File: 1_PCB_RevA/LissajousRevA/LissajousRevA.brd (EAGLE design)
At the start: 100 x 80 mm, 77 parts, among them U101 LM348D, U201 LM348D, U401 LM348D

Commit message: quick route
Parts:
- moved C505 6.35 mm to (17.8, 16.5)
- moved C504 5.39 mm to (12.7, 16.5)
- moved Q503 4.58 mm to (22.9, 16.5)
- moved R508 2.54 mm to (12.7, 22.9)
- moved R509 2.54 mm to (7.62, 22.9), turned to 270 degrees
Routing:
- net N$39: track 28.0 -> 6.56 mm, vias 2 -> 0
- net N$46: track 30.3 -> 17.8 mm
- net N$45: track 23.9 -> 14.6 mm
- net N$40: track 11.1 -> 7.90 mm
- net N$38: track 158.6 -> 156.3 mm
- net N$42: track 43.5 -> 42.0 mm
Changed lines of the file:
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@@
 <element name="R506" library="passives" package="0603-RES" value="33K" x="53.34" y="29.21" rot="R90"/>
 <element name="Q502" library="adafruit" package="SOT23" value="" x="53.34" y="48.26" rot="R90"/>
-<element name="C504" library="passives" package="0603-CAP" value="10nF" x="8.89" y="20.32" rot="R270"/>
+<element name="C504" library="passives" package="0603-CAP" value="10nF" x="12.7" y="16.51" rot="R270"/>
 <element name="R507" library="passives" package="0603-RES" value="33K" x="38.1" y="16.51" rot="R90"/>
-<element name="C505" library="passives" package="0603-CAP" value="10nF" x="12.7" y="20.32" rot="R90"/>
-<element name="Q503" library="adafruit" package="SOT23" value="" x="19.05" y="13.97" rot="R90"/>
-<element name="R508" library="passives" package="0603-RES" value="33K" x="12.7" y="25.4" rot="R90"/>
-<element name="R509" library="passives" package="0603-RES" value="33K" x="7.62" y="25.4" rot="R90"/>
+<element name="C505" library="passives" package="0603-CAP" value="10nF" x="17.78" y="16.51" rot="R90"/>
+<element name="Q503" library="adafruit" package="SOT23" value="" x="22.86" y="16.51" rot="R90"/>
+<element name="R508" library="passives" package="0603-RES" value="33K" x="12.7" y="22.86" rot="R90"/>
+<element name="R509" library="passives" package="0603-RES" value="33K" x="7.62" y="22.86" rot="R270"/>
 <element name="R510" library="passives" package="0603-RES" value="33K" x="7.62" y="50.8" rot="R270"/>
 <element name="TP305" library="passives" package="TP_15TH" value="TEST-POINTTP_15TH_THRU" x="2.54" y="41.91"/>
@@
 <wire x1="88.9" y1="31.75" x2="88.9" y2="44.45" width="0.4064" layer="16"/>
 <wire x1="88.9" y1="44.45" x2="86.36" y2="46.99" width="0.4064" layer="16"/>
-<wire x1="33.02" y1="26.67" x2="33.02" y2="26.67" width="0" layer="19" extent="1-16"/>
-<wire x1="33.02" y1="26.67" x2="33.02" y2="29.21" width="0" layer="19" extent="1-16"/>
-<wire x1="33.02" y1="29.21" x2="36.83" y2="33.02" width="0" layer="19" extent="1-16"/>
 <via x="36.83" y="33.02" extent="1-16" drill="0.6"/>
 <wire x1="17.78" y1="35.4838" x2="17.78" y2="39.79" width="0.4064" layer="1"/>
 <wire x1="17.78" y1="39.79" x2="16.09" y2="39.79" width="0.4064" layer="1"/>
 <wire x1="16.09" y1="39.79" x2="15.24" y2="40.64" width="0.4064" layer="1"/>
-<wire x1="33.02" y1="29.21" x2="33.02" y2="31.75" width="0" layer="19" extent="1-16"/>
 <wire x1="33.02" y1="31.75" x2="31.75" y2="33.02" width="0.4064" layer="16"/>
 <wire x1="31.75" y1="33.02" x2="6.35" y2="33.02" width="0.4064" layer="16"/>
@@
 <wire x1="33.02" y1="3.81" x2="35.56" y2="1.27" width="0.4064" layer="1"/>
 <wire x1="35.56" y1="1.27" x2="55.88" y2="1.27" width="0.4064" layer="1"/>
-<wire x1="33.02" y1="3.81" x2="33.02" y2="26.67" width="0" layer="19" extent="1-1"/>
+<wire x1="33.02" y1="31.75" x2="36.83" y2="33.02" width="0" layer="19" extent="16-16"/>
+<wire x1="68.58" y1="41.06" x2="43.18" y2="38.1" width="0" layer="19" extent="1-1"/>
 </signal>
 <signal name="0V">
@@
 <wire x1="34.29" y1="42.76" x2="34.29" y2="43.18" width="0" layer="19" extent="1-1"/>
 <wire x1="38.1" y1="15.66" x2="34.29" y2="20.32" width="0" layer="19" extent="1-1"/>
-<wire x1="20.15" y1="14.92" x2="34.29" y2="20.32" width="0" layer="19" extent="1-1"/>
-<wire x1="17.78" y1="21.59" x2="20.15" y2="14.92" width="0" layer="19" extent="1-1"/>
+<wire x1="23.96" y1="17.46" x2="34.29" y2="20.32" width="0" layer="19" extent="1-1"/>
+<wire x1="17.78" y1="21.59" x2="23.96" y2="17.46" width="0" layer="19" extent="1-1"/>
 </signal>
 <signal name="N$8">
@@
 <wire x1="17.78" y1="26.25" x2="20.32" y2="28.79" width="0.4064" layer="1"/>
 <wire x1="20.32" y1="28.79" x2="20.32" y2="30.5562" width="0.4064" layer="1"/>
-<wire x1="24.13" y1="26.25" x2="17.78" y2="26.25" width="0" layer="19" extent="1-16"/>
-<wire x1="19.05" y1="24.98" x2="24.55" y2="26.25" width="0" layer="19" extent="1-16"/>
-<wire x1="24.55" y1="26.25" x2="24.13" y2="26.25" width="0" layer="19" extent="1-1"/>
+<wire x1="19.05" y1="24.98" x2="17.78" y2="26.25" width="0" layer="19" extent="1-1"/>
 </signal>
 <signal name="N$15">
@@
 <contactref element="U401" pad="14"/>
 <contactref element="C504" pad="2"/>
-<wire x1="8.89" y1="19.47" x2="8.89" y2="17.78" width="0.4064" layer="1"/>
-<wire x1="8.89" y1="17.78" x2="10.16" y2="16.51" width="0.4064" layer="1"/>
-<via x="10.16" y="16.51" extent="1-16" drill="0.6"/>
-<wire x1="48.26" y1="16.51" x2="55.88" y2="24.13" width="0.4064" layer="16"/>
 <wire x1="53.34" y1="30.06" x2="47.4862" y2="30.06" width="0.4064" layer="1"/>
 <wire x1="47.4862" y1="30.06" x2="46.99" y2="30.5562" width="0.4064" layer="1"/>
-<wire x1="55.88" y1="24.13" x2="55.88" y2="26.67" width="0.4064" layer="16"/>
-<via x="55.88" y="26.67" extent="1-16" drill="0.6"/>
-<wire x1="55.88" y1="26.67" x2="55.88" y2="27.94" width="0.4064" layer="1"/>
-<wire x1="53.34" y1="30.06" x2="53.76" y2="30.06" width="0.4064" layer="1"/>
-<wire x1="53.76" y1="30.06" x2="55.88" y2="27.94" width="0.4064" layer="1"/>
-<wire x1="10.16" y1="16.51" x2="48.26" y2="16.51" width="0" layer="19" extent="1-16"/>
+<wire x1="12.7" y1="15.66" x2="14.39" y2="15.66" width="0" layer="19" extent="1-16"/>
+<wire x1="14.39" y1="15.66" x2="15.24" y2="16.51" width="0" layer="19" extent="1-16"/>
+<wire x1="15.24" y1="16.51" x2="46.99" y2="30.5562" width="0" layer="19" extent="1-16"/>
 </signal>
 <signal name="N$42">
@@
 <contactref element="C505" pad="2"/>
 <contactref element="R508" pad="1"/>
-<wire x1="12.7" y1="21.17" x2="12.7" y2="24.55" width="0.4064" layer="1"/>
-<wire x1="12.7" y1="21.17" x2="8.89" y2="21.17" width="0.4064" layer="1"/>
 <wire x1="6.35" y1="20.32" x2="5.08" y2="21.59" width="0.4064" layer="16"/>
 <via x="5.08" y="21.59" extent="1-16" drill="0.6"/>
-<wire x1="5.08" y1="21.59" x2="8.47" y2="21.59" width="0.4064" layer="1"/>
-<wire x1="8.47" y1="21.59" x2="8.89" y2="21.17" width="0.4064" layer="1"/>
 <wire x1="6.35" y1="20.32" x2="36.83" y2="20.32" width="0.4064" layer="16"/>
 <wire x1="36.83" y1="20.32" x2="38.1" y2="17.36" width="0" layer="19" extent="1-16"/>
+<wire x1="12.7" y1="17.36" x2="6.35" y2="20.32" width="0" layer="19" extent="1-16"/>
+<wire x1="17.78" y1="17.36" x2="12.7" y2="17.36" width="0.4064" layer="1"/>
+<wire x1="12.7" y1="22.01" x2="12.7" y2="17.36" width="0.4064" layer="1"/>
 </signal>
 <signal name="N$45">
@@
 <wire x1="16.51" y1="27.94" x2="16.51" y2="30.5562" width="0.4064" layer="1"/>
 <wire x1="16.51" y1="31.75" x2="16.51" y2="30.5562" width="0.4064" layer="1"/>
-<wire x1="12.7" y1="19.47" x2="15.24" y2="22.01" width="0.4064" layer="1"/>
 <wire x1="15.24" y1="22.01" x2="15.24" y2="25.4" width="0.4064" layer="1"/>
-<wire x1="17.95" y1="13.97" x2="13.97" y2="13.97" width="0.4064" layer="1"/>
-<wire x1="13.97" y1="13.97" x2="12.7" y2="15.24" width="0.4064" layer="1"/>
-<wire x1="12.7" y1="15.24" x2="12.7" y2="19.47" width="0.4064" layer="1"/>
+<wire x1="17.78" y1="15.66" x2="20.91" y2="15.66" width="0.4064" layer="1"/>
+<wire x1="20.91" y1="15.66" x2="21.76" y2="16.51" width="0.4064" layer="1"/>
+<wire x1="17.78" y1="15.66" x2="15.24" y2="22.01" width="0" layer="19" extent="1-1"/>
 </signal>
 <signal name="N$40">
@@
 <contactref element="U201" pad="9"/>
 <wire x1="15.24" y1="30.5562" x2="15.24" y2="28.79" width="0.4064" layer="1"/>
-<wire x1="15.24" y1="28.79" x2="12.7" y2="26.25" width="0.4064" layer="1"/>
-<wire x1="7.62" y1="24.55" x2="9.31" y2="24.55" width="0.4064" layer="1"/>
-<wire x1="12.7" y1="26.25" x2="11.01" y2="26.25" width="0.4064" layer="1"/>
-<wire x1="11.01" y1="26.25" x2="9.31" y2="24.55" width="0.4064" layer="1"/>
+<wire x1="7.62" y1="23.71" x2="9.31" y2="24.55" width="0" layer="19" extent="1-16"/>
+<wire x1="12.7" y1="23.71" x2="11.01" y2="26.25" width="0" layer="19" extent="1-16"/>
+<wire x1="11.01" y1="26.25" x2="9.31" y2="24.55" width="0" layer="19" extent="1-16"/>
+<wire x1="12.7" y1="23.71" x2="12.7" y2="26.25" width="0.4064" layer="1"/>
+<wire x1="12.7" y1="26.25" x2="15.24" y2="28.79" width="0.4064" layer="1"/>
 </signal>
 <signal name="N$46">
@@
 <contactref element="C506" pad="1"/>
 <contactref element="U201" pad="8"/>
-<wire x1="7.62" y1="26.25" x2="7.62" y2="27.94" width="0.4064" layer="1"/>
-<wire x1="7.62" y1="27.94" x2="10.16" y2="30.48" width="0.4064" layer="1"/>
+<wire x1="7.62" y1="22.01" x2="7.62" y2="27.94" width="0" layer="19" extent="1-16"/>
+<wire x1="7.62" y1="27.94" x2="10.16" y2="30.48" width="0" layer="19" extent="1-16"/>
 <wire x1="10.16" y1="30.48" x2="13.8938" y2="30.48" width="0.4064" layer="1"/>
 <wire x1="13.8938" y1="30.48" x2="13.97" y2="30.5562" width="0.4064" layer="1"/>
 <wire x1="7.62" y1="44.87" x2="7.62" y2="44.45" width="0.4064" layer="1"/>
-<wire x1="7.62" y1="27.94" x2="2.54" y2="33.02" width="0.4064" layer="1"/>
+<wire x1="7.62" y1="27.94" x2="2.54" y2="33.02" width="0" layer="19" extent="1-16"/>
 <wire x1="2.54" y1="33.02" x2="2.54" y2="39.37" width="0.4064" layer="1"/>
 <wire x1="2.54" y1="39.37" x2="7.62" y2="44.45" width="0.4064" layer="1"/>
@@
 <contactref element="R503" pad="2"/>
 <contactref element="Q501" pad="1"/>
-<wire x1="20.15" y1="13.02" x2="22.54" y2="13.02" width="0.4064" layer="1"/>
 <wire x1="22.54" y1="13.02" x2="22.86" y2="12.7" width="0.4064" layer="1"/>
 <via x="22.86" y="12.7" extent="1-16" drill="0.6"/>
@@
 <via x="64.77" y="11.43" extent="1-16" drill="0.6"/>
 <wire x1="64.77" y1="11.43" x2="64.77" y2="6.58" width="0.4064" layer="1"/>
+<wire x1="22.54" y1="13.02" x2="23.96" y2="15.56" width="0" layer="19" extent="1-1"/>
 </signal>
 </signals>

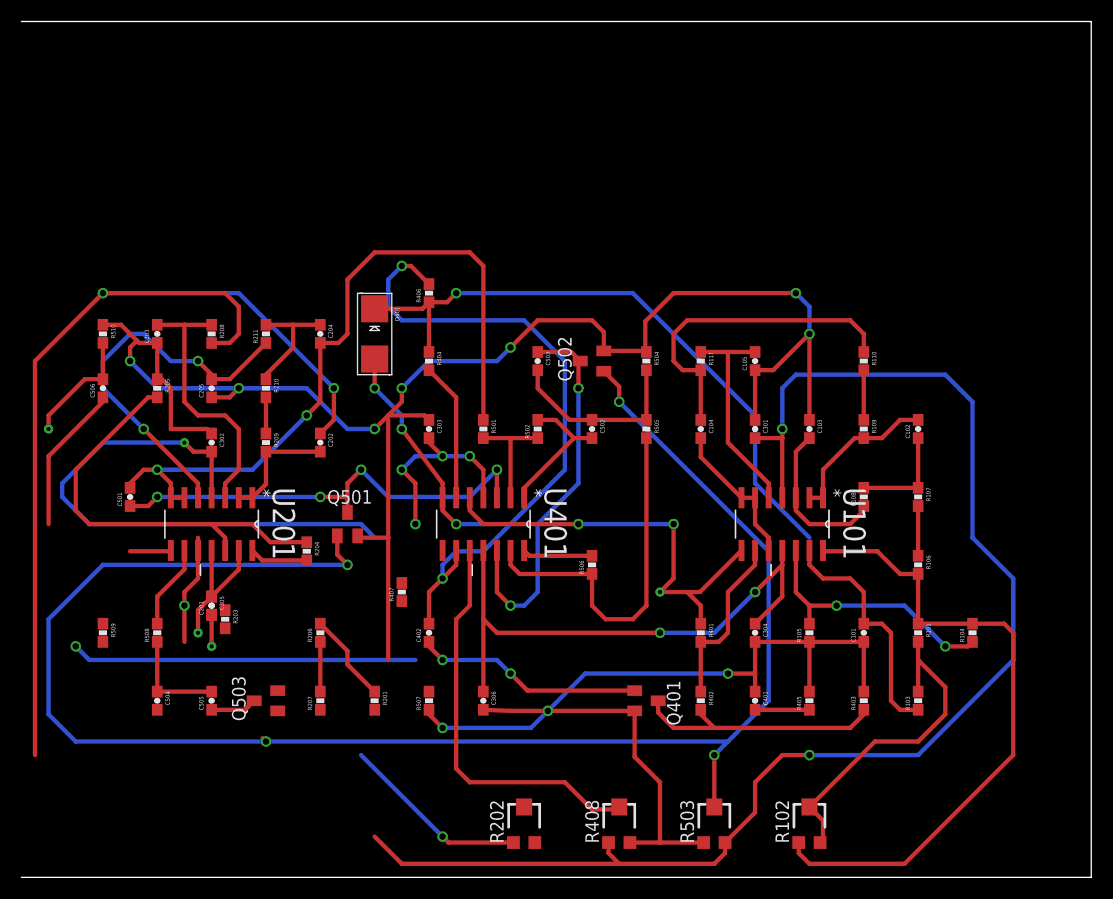
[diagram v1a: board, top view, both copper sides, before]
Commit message: layout in bottom left
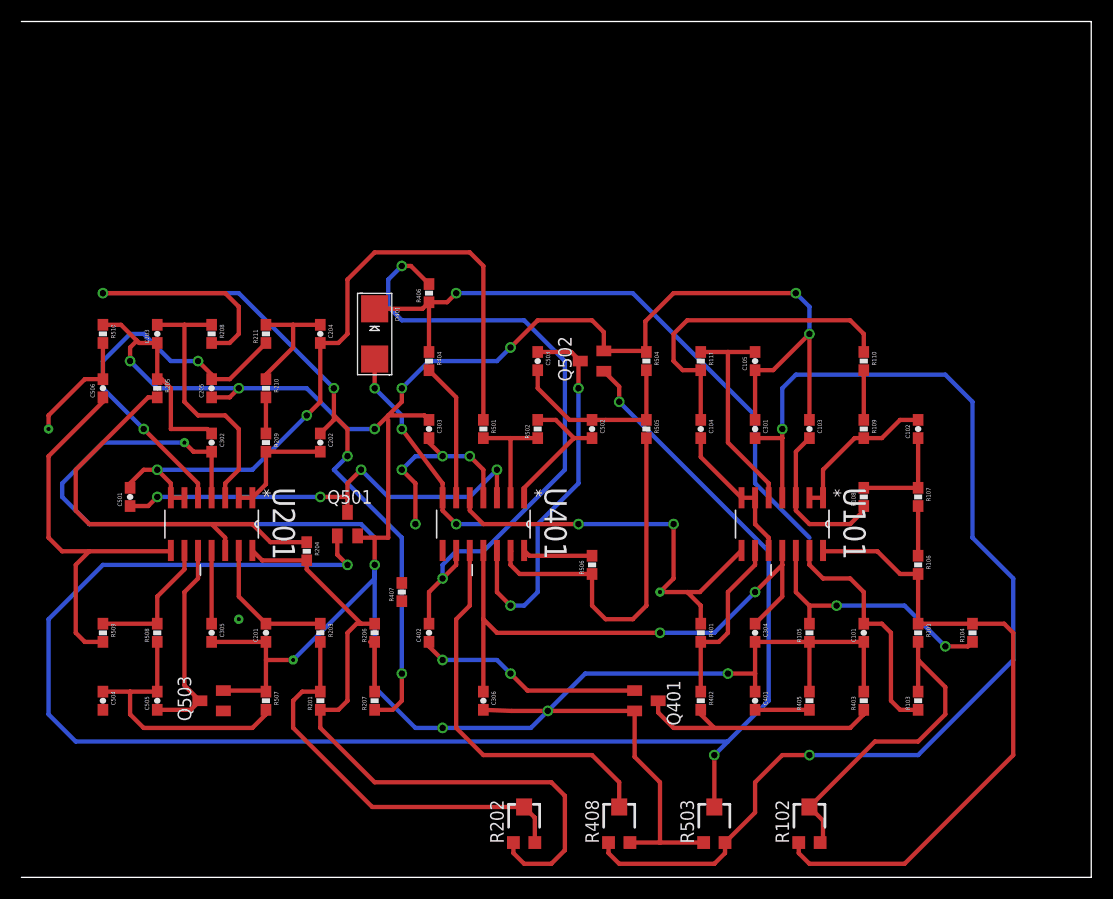
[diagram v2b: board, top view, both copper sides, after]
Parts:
- moved R507 15.2 mm to (22.9, 16.5), turned to 270 degrees
- moved R203 8.98 mm to (27.9, 22.9)
- moved TP303 7.73 mm to (25.4, 20.3)
- moved C201 5.68 mm to (22.9, 22.9)
- moved C505 5.08 mm to (12.7, 16.5)
- moved R201 5.08 mm to (27.9, 16.5), turned to 90 degrees
- moved R206 5.08 mm to (33.0, 22.9)
- moved R207 5.08 mm to (33.0, 16.5)
- moved C504 5.08 mm to (7.62, 16.5)
- moved Q503 5.08 mm to (17.8, 16.5)
- moved TP302 4.02 mm to (20.3, 24.1)
- moved C305 2.54 mm to (17.8, 22.9)
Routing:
- net N$24: track 0.00 -> 38.5 mm
- net 0V: track 247.4 -> 281.1 mm, vias 10 -> 11
- net N$15: track 31.5 -> 64.6 mm, vias 1 -> 0
- net V+: track 202.5 -> 178.6 mm
- net N$46: track 17.8 -> 38.2 mm
- net N$42: track 42.0 -> 26.0 mm, vias 1 -> 0
- net N$17: track 94.5 -> 81.9 mm, vias 2 -> 4
- net N$10: track 5.36 -> 13.0 mm
- net N$40: track 7.90 -> 13.0 mm
- net N$45: track 14.6 -> 19.5 mm, vias 1 -> 0
- net V-: track 60.4 -> 59.0 mm
- net N$34: track 37.8 -> 37.1 mm
- net N$38: track 156.3 -> 155.8 mm, vias 4 -> 3

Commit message: more sparse routing
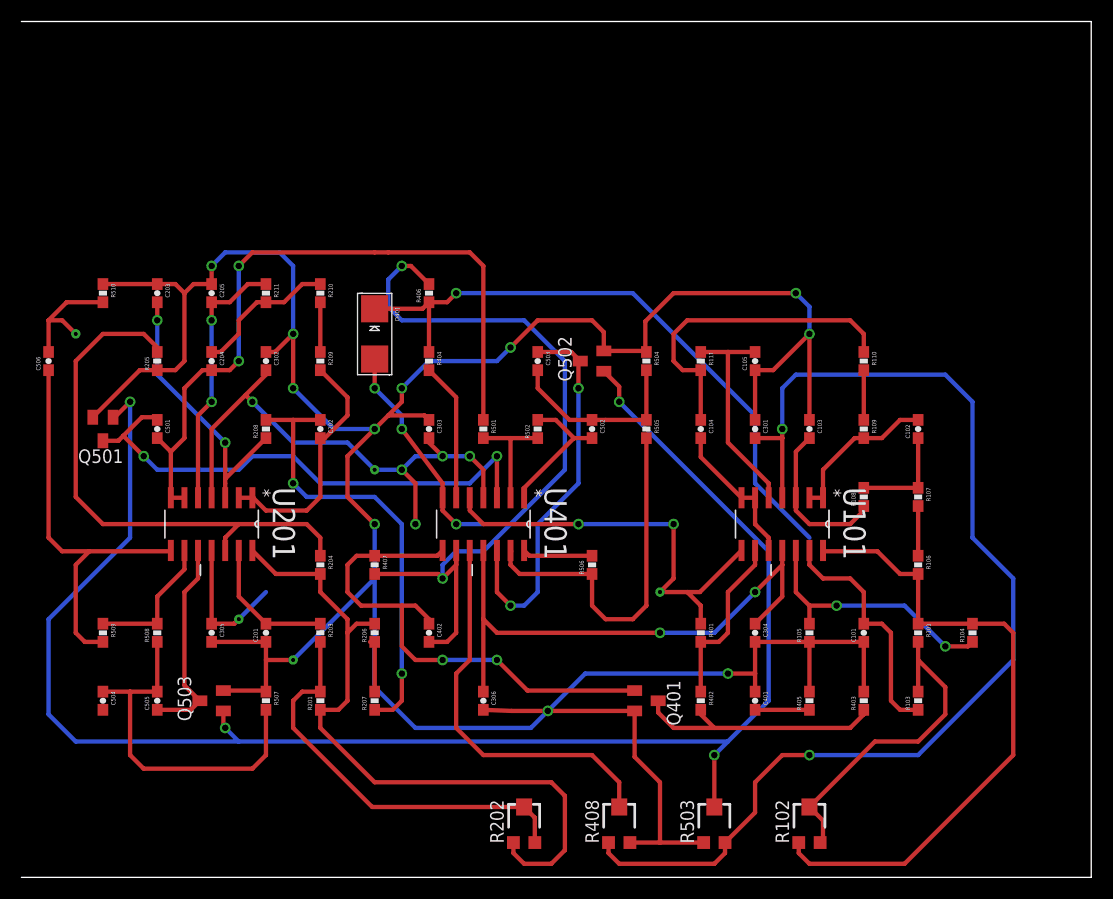
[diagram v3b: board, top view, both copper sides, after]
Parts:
- moved Q501 24.5 mm to (7.62, 41.9), turned to 180 degrees
- moved TP301 18.0 mm to (33.0, 38.1)
- moved C204 10.5 mm to (17.8, 48.3)
- moved R208 10.2 mm to (22.9, 41.9), turned to 90 degrees
- moved R210 10.2 mm to (27.9, 54.6)
- moved TP305 9.25 mm to (5.08, 50.8)
- moved R209 9.16 mm to (27.9, 48.3)
- moved C302 9.16 mm to (22.9, 48.3)
- moved C205 8.89 mm to (17.8, 54.6), turned to 270 degrees
- moved C501 6.84 mm to (12.7, 41.9), turned to 270 degrees
- moved C506 5.68 mm to (2.54, 48.3)
- moved C203 3.81 mm to (12.7, 54.6), turned to 270 degrees
- moved R211 3.81 mm to (22.9, 54.6), turned to 270 degrees
- moved R510 3.81 mm to (7.62, 54.6)
- moved R407 3.59 mm to (33.0, 29.2), turned to 270 degrees
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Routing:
- net N$17: track 81.9 -> 42.2 mm, vias 4 -> 2
- net N$32: track 21.4 -> 48.4 mm
- net V+: track 178.6 -> 157.8 mm, vias 6 -> 7
- net N$25: track 60.6 -> 73.0 mm
- net N$21: track 11.2 -> 22.9 mm
- net N$18: track 36.1 -> 24.6 mm
- net N$9: track 40.0 -> 51.4 mm
- net 0V: track 281.1 -> 291.2 mm
- net N$42: track 26.0 -> 34.1 mm
- net V-: track 59.0 -> 65.3 mm
- net N$20: track 42.6 -> 48.9 mm, vias 4 -> 2
- net N$38: track 155.8 -> 151.8 mm, vias 3 -> 4
- net N$19: track 11.2 -> 14.0 mm
- net N$23: track 3.38 -> 4.65 mm
- net N$16: track 25.4 -> 26.3 mm, vias 0 -> 2
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
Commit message: fully routed and pass board house drc
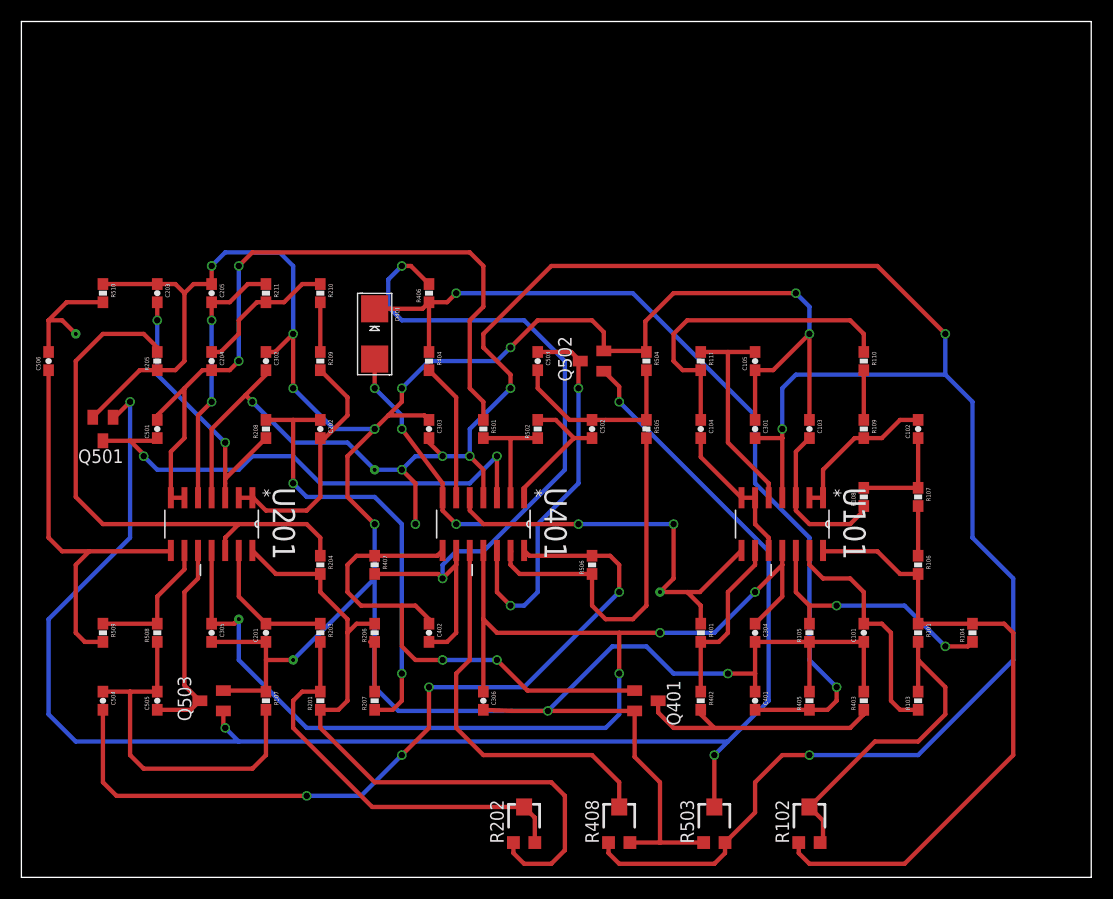
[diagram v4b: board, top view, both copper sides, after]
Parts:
- turned C501 to 90 degrees
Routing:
- net N$39: track 6.56 -> 77.7 mm, vias 0 -> 4
- net V+: track 157.8 -> 224.1 mm, vias 7 -> 9
- net V-: track 65.3 -> 111.9 mm, vias 2 -> 3
- net N$30: track 64.2 -> 83.3 mm, vias 1 -> 2
- net SINEGEN2: track 67.2 -> 70.4 mm
- net N$20: track 48.9 -> 47.2 mm
- net 0V: track 291.2 -> 292.0 mm

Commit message: more layout opt
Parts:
- moved TP304 13.5 mm to (68.6, 36.8)
- moved C303 12.0 mm to (49.5, 45.7)
- moved R501 12.0 mm to (49.5, 52.1)
- moved C101 7.41 mm to (85.1, 26.7)
- moved C102 7.41 mm to (90.2, 45.7)
- moved C103 7.41 mm to (80.0, 45.7)
- moved C105 7.41 mm to (74.9, 52.1)
- moved C301 7.41 mm to (74.9, 45.7)
- moved C304 7.41 mm to (74.9, 26.7)
- moved R101 7.41 mm to (90.2, 26.7)
- moved R102 7.41 mm to (80.0, 8.89)
- moved R105 7.41 mm to (80.0, 26.7)
- moved R106 7.41 mm to (90.2, 33.0)
- moved R109 7.41 mm to (85.1, 45.7)
- moved R110 7.41 mm to (85.1, 52.1)
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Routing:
- net V+: track 224.1 -> 273.2 mm, vias 9 -> 5
- net N$38: track 151.8 -> 130.9 mm
- net N$13: track 16.3 -> 31.7 mm
- net N$25: track 73.0 -> 59.5 mm
- net 0V: track 292.0 -> 283.1 mm
- net N$7: track 60.8 -> 54.9 mm
- net SINEGEN2: track 70.4 -> 65.1 mm
- net N$28: track 20.8 -> 15.6 mm, vias 3 -> 0
- net N$37: track 34.2 -> 29.1 mm
- net N$26: track 10.7 -> 15.5 mm
- net VIEW1: track 40.4 -> 35.5 mm
- net V-: track 111.9 -> 107.1 mm
- net N$30: track 83.3 -> 79.1 mm
- net N$16: track 26.3 -> 29.3 mm
- net N$20: track 47.2 -> 49.4 mm
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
